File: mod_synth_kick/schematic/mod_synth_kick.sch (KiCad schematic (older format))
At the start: 33 parts

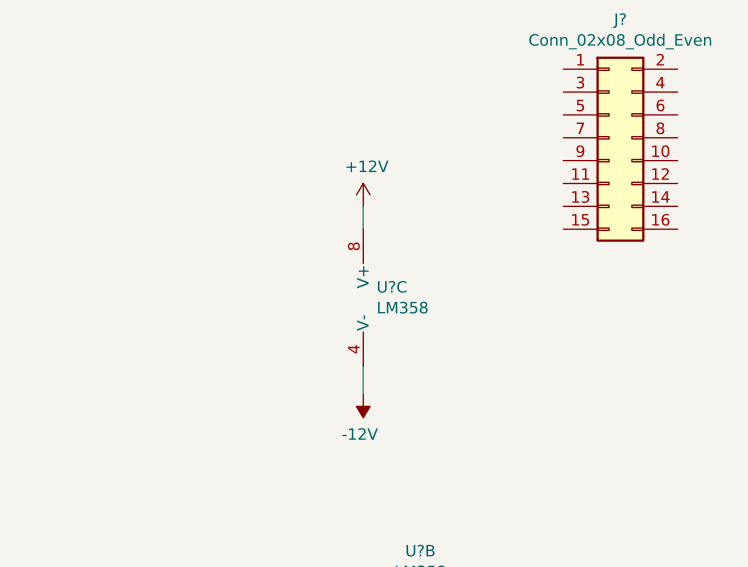
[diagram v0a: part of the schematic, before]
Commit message: Add decoupling for op amp
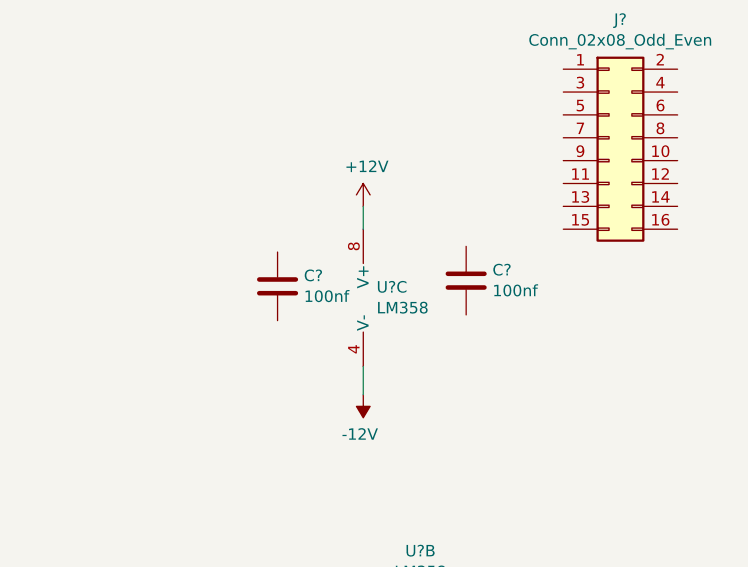
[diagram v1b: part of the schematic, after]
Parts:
- added C? (x2): 100nf, symbol Device:C
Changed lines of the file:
@@
 EESchema Schematic File Version 4
+LIBS:mod_synth_kick-cache
 EELAYER 29 0
 EELAYER END
@@
 Wire Wire Line
 	1425 1975 1425 1925
+$Comp
+L Device:C C?
+U 1 1 5D5D6113
+P 9050 3600
+F 0 "C?" H 8935 3554 50  0000 R CNN
+F 1 "100nf" H 8935 3645 50  0000 R CNN
+F 2 "" H 9088 3450 50  0001 C CNN
+F 3 "~" H 9050 3600 50  0001 C CNN
+	1    9050 3600
+	-1   0    0    1
+$EndComp
+$Comp
+L Device:C C?
+U 1 1 5D5D6965
+P 9875 3575
+F 0 "C?" H 9760 3529 50  0000 R CNN
+F 1 "100nf" H 9760 3620 50  0000 R CNN
+F 2 "" H 9913 3425 50  0001 C CNN
+F 3 "~" H 9875 3575 50  0001 C CNN
+	1    9875 3575
+	-1   0    0    1
+$EndComp
 $EndSCHEMATC

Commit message: Attempt to layout PCB
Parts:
- added C10, C9: 10uf, Capacitor_THT:CP_Radial_D5.0mm_P2.00mm, symbol Device:CP
- added J4, J5: Conn_01x05_Female, Connector_PinSocket_2.54mm:PinSocket_1x05_P2.54mm_Vertical, symbol Connector:Conn_01x05_Female
- added J6, J7: Conn_01x05_Male, Connector_PinHeader_2.54mm:PinHeader_1x05_P2.54mm_Vertical, symbol Connector:Conn_01x05_Male
- C1, C2, C3, C4, C5, C7, C8: renamed from C?; footprint (none) -> Capacitor_THT:C_Disc_D9.0mm_W2.5mm_P5.00mm
- C6: renamed from C?; footprint (none) -> Capacitor_THT:CP_Radial_D5.0mm_P2.00mm
- J1: renamed from J?; value AudioJack2 -> Trigger; footprint (none) -> Connector_Audio:Jack_3.5mm_QingPu_WQP-PJ398SM_Vertical_CircularHoles
- J2: renamed from J?; value AudioJack2 -> Out; footprint (none) -> Connector_Audio:Jack_3.5mm_QingPu_WQP-PJ398SM_Vertical_CircularHoles
- J3: renamed from J?; footprint (none) -> Connector_IDC:IDC-Header_2x08_P2.54mm_Vertical
- R1, R10, R11, R12, R13, R14, R2, R3, R4, R5, R6, R7, R8, R9: renamed from R?; footprint (none) -> Resistor_THT:R_Axial_DIN0207_L6.3mm_D2.5mm_P10.16mm_Horizontal
- RV1, RV2: renamed from RV?; footprint (none) -> Potentiometer_THT:Potentiometer_Alpha_RD901F-40-00D_Single_Vertical_CircularHoles
- SW1: renamed from SW?; footprint (none) -> Connector_PinHeader_2.54mm:PinHeader_1x02_P2.54mm_Vertical
- U1: renamed from U?; footprint (none) -> Package_DIP:DIP-8_W7.62mm_Socket_LongPads
- gave numbers to parts that had none: 5
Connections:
- net +12V: now also C8.2, J3.10 (Pin_10), J3.9 (Pin_9), C10.2
- net -12V: now also C7.1, J3.1 (Pin_1), J3.2 (Pin_2), C9.2
- net GND: now also C7.2, C8.1, J3.3 (Pin_3), J3.4 (Pin_4), J3.5 (Pin_5), J3.6 (Pin_6), J3.7 (Pin_7), J3.8 (Pin_8), C10.1, C9.1, J4.1 (Pin_1), J5.1 (Pin_1); no longer J1.S, J2.S, RV1.1, RV1.2, RV2.1, RV2.2
- net OUT_PCB_A: now reaches C6.2
- net OUT_PCB_A: now also J5.2 (Pin_2); no longer J2.T
- net DECAY_PCB_A: now reaches C4.2
- net DECAY_PCB_A: now also J4.2 (Pin_2); no longer R11.1
- net FREQ_PCB_A: now reaches R9.1
- net FREQ_PCB_A: now also J4.4 (Pin_4); no longer RV1.3
- net IN_PCB_A: now reaches R2.1
- net IN_PCB_A: now also J4.3 (Pin_3); no longer J1.T
- new net DECAY_PCB_B: J6.2 (Pin_2), R11.1
- new net FREQ_PCB_B: J6.4 (Pin_4), RV1.3
- new net GND_PCB_B: J1.S, J2.S, J6.1 (Pin_1), J7.1 (Pin_1), RV1.1, RV1.2, RV2.1, RV2.2
- new net IN_PCB_B: J1.T, J6.3 (Pin_3)
- new net OUT_PCB_B: J2.T, J7.2 (Pin_2)
- no-connect marks 0 -> 3
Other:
- moved on the sheet: C7, C8, J1, J3, RV1, U1C

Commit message: Layout and add LED to Kick
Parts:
- added D3: LED, LED_THT:LED_D5.0mm, symbol Device:LED
- added R15: 1k, Resistor_THT:R_Axial_DIN0207_L6.3mm_D2.5mm_P10.16mm_Horizontal, symbol Device:R
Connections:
- net GND_PCB_B: now also R15.1
- net LED_PCB_A: now reaches C2.2, Q2.1 (C), R5.1
- net LED_PCB_A: now also J4.5 (Pin_5)
- net LED_PCB_B: now reaches J6.5 (Pin_5)
- net LED_PCB_B: now also D3.2 (A)
- new net: D3.1 (K), R15.2
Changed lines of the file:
@@
 	2750 1600 2750 1475
-Wire Wire Line
-	3275 1775 3650 1775
 Wire Wire Line
 	8600 1700 8600 1775
@@
 Wire Wire Line
 	3100 4275 3250 4275
+$Comp
+L Device:LED D3
+U 1 1 5D5ED36A
+P 3600 2725
+F 0 "D3" V 3639 2608 50  0000 R CNN
+F 1 "LED" V 3548 2608 50  0000 R CNN
+F 2 "LED_THT:LED_D5.0mm" H 3600 2725 50  0001 C CNN
+F 3 "~" H 3600 2725 50  0001 C CNN
+	1    3600 2725
+	0    -1   -1   0
+$EndComp
+$Comp
+L Device:R R15
+U 1 1 5D5EE20F
+P 3600 3125
+F 0 "R15" H 3530 3079 50  0000 R CNN
+F 1 "1k" H 3530 3170 50  0000 R CNN
+F 2 "Resistor_THT:R_Axial_DIN0207_L6.3mm_D2.5mm_P10.16mm_Horizontal" V 3530 3125 50  0001 C CNN
+F 3 "~" H 3600 3125 50  0001 C CNN
+	1    3600 3125
+	-1   0    0    1
+$EndComp
+Wire Wire Line
+	3600 2975 3600 2875
+Wire Wire Line
+	3600 3275 3600 3375
+Wire Wire Line
+	3275 1775 3600 1775
+Text Label 3600 2025 0    50   ~ 0
+LED_PCB_A
+Text Label 3600 2175 0    50   ~ 0
+LED_PCB_B
+Wire Wire Line
+	3600 2175 3600 2575
+Wire Wire Line
+	3600 2025 3600 1775
+Connection ~ 3600 1775
+Wire Wire Line
+	3600 1775 3650 1775
+Text Label 3250 4375 0    50   ~ 0
+LED_PCB_B
+Text Label 2450 4375 2    50   ~ 0
+LED_PCB_A
+Wire Wire Line
+	2450 4375 2650 4375
+Wire Wire Line
+	3100 4375 3250 4375
+Text Label 3600 3375 0    50   ~ 0
+GND_PCB_B
 $EndSCHEMATC

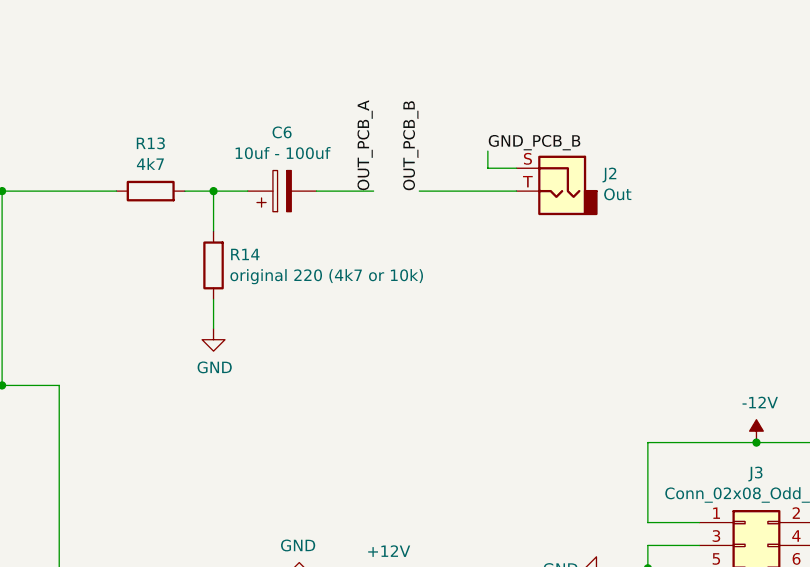
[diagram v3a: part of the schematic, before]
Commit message: Fix resistor location
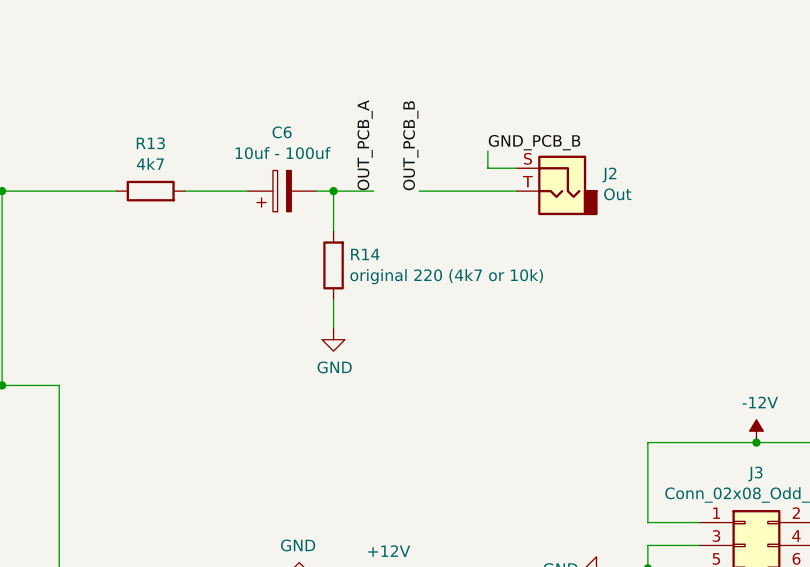
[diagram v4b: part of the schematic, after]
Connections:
- net OUT_PCB_A: now also R14.2
- net at C6.1, R13.2: no longer R14.2
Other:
- moved on the sheet: R14
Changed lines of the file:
@@
 L Device:R R14
 U 1 1 5D5FAF1F
-P 7400 2200
-F 0 "R14" H 7330 2154 50  0000 R CNN
-F 1 "original 220 (4k7 or 10k)" H 7330 2245 50  0000 R CNN
-F 2 "Resistor_THT:R_Axial_DIN0207_L6.3mm_D2.5mm_P10.16mm_Horizontal" V 7330 2200 50  0001 C CNN
-F 3 "~" H 7400 2200 50  0001 C CNN
-	1    7400 2200
+P 7925 2200
+F 0 "R14" H 7855 2154 50  0000 R CNN
+F 1 "original 220 (4k7 or 10k)" H 7855 2245 50  0000 R CNN
+F 2 "Resistor_THT:R_Axial_DIN0207_L6.3mm_D2.5mm_P10.16mm_Horizontal" V 7855 2200 50  0001 C CNN
+F 3 "~" H 7925 2200 50  0001 C CNN
+	1    7925 2200
 	-1   0    0    1
 $EndComp
@@
 L power:GND #PWR0101
 U 1 1 5D5FB3E2
-P 7400 2475
-F 0 "#PWR0101" H 7400 2225 50  0001 C CNN
-F 1 "GND" H 7405 2302 50  0000 C CNN
-F 2 "" H 7400 2475 50  0001 C CNN
-F 3 "" H 7400 2475 50  0001 C CNN
-	1    7400 2475
+P 7925 2475
+F 0 "#PWR0101" H 7925 2225 50  0001 C CNN
+F 1 "GND" H 7930 2302 50  0000 C CNN
+F 2 "" H 7925 2475 50  0001 C CNN
+F 3 "" H 7925 2475 50  0001 C CNN
+	1    7925 2475
 	1    0    0    -1
 $EndComp
@@
 Connection ~ 6475 1875
 Wire Wire Line
-	7275 1875 7400 1875
-Wire Wire Line
-	7400 2050 7400 1875
-Connection ~ 7400 1875
-Wire Wire Line
-	7400 1875 7550 1875
-Wire Wire Line
-	7400 2475 7400 2350
+	7925 2050 7925 1875
+Wire Wire Line
+	7925 2475 7925 2350
 $Comp
 L Amplifier_Operational:LM358 U1
@@
 	8300 1875 8725 1875
 Wire Wire Line
-	7850 1875 8100 1875
+	7850 1875 7925 1875
 Text Label 1125 2075 3    50   ~ 0
 IN_PCB_B
@@
 Text Label 3600 3375 0    50   ~ 0
 GND_PCB_B
+Connection ~ 7925 1875
+Wire Wire Line
+	7925 1875 8100 1875
+Wire Wire Line
+	7275 1875 7550 1875
 $EndSCHEMATC

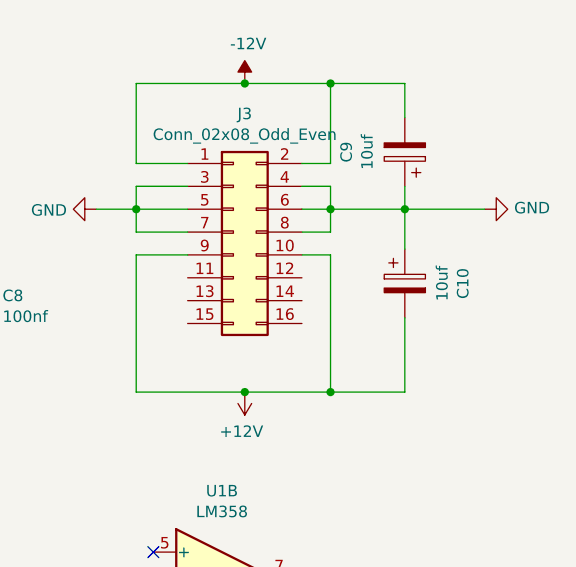
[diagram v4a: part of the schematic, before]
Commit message: Fix reversed capacitor
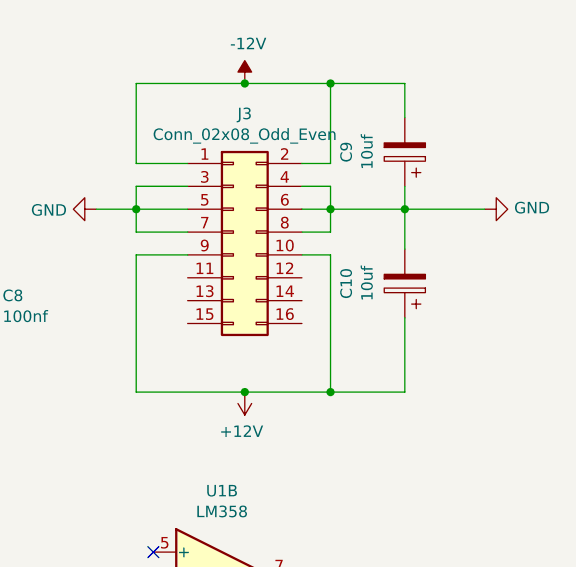
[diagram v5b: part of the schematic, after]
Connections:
- net +12V: now also C10.1; no longer C10.2
- net GND: now also C10.2; no longer C10.1
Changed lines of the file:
@@
 F 3 "~" H 10475 3850 50  0001 C CNN
 	1    10475 3850
-	1    0    0    -1
+	-1   0    0    1
 $EndComp
 Connection ~ 8150 3700
